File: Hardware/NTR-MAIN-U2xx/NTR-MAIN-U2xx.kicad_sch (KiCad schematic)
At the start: 14 parts, among them J1 Conn_01x15, J2 Conn_01x15, J3 Conn_01x05

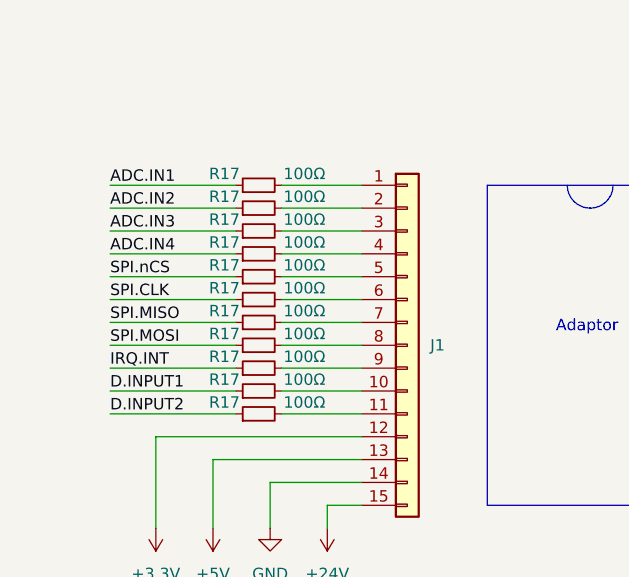
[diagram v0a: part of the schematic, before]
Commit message: update bootloader
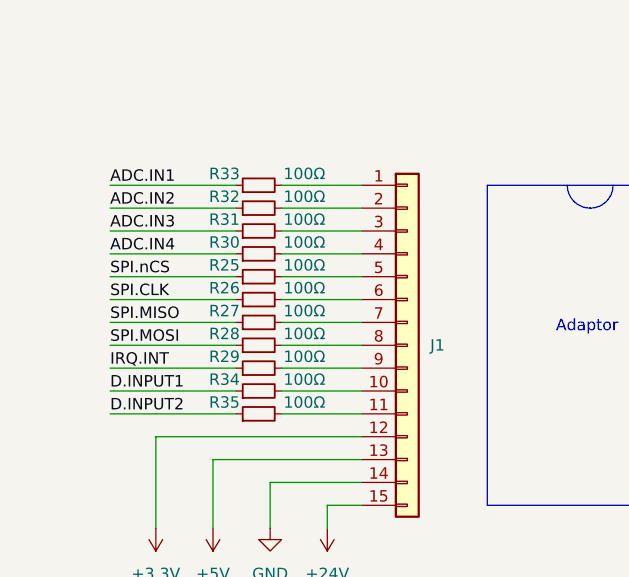
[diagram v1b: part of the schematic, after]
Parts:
- renumbered R17 to R25, R17 to R26, R17 to R27, R17 to R28, R17 to R29, R17 to R30, R17 to R31, R17 to R32, R17 to R33, R17 to R34, R17 to R35
